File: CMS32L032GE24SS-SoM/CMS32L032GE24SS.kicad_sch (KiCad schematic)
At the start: 9 parts, among them J101 Conn_01x12, J102 Conn_01x12, U101 CMS32L032GE24SS

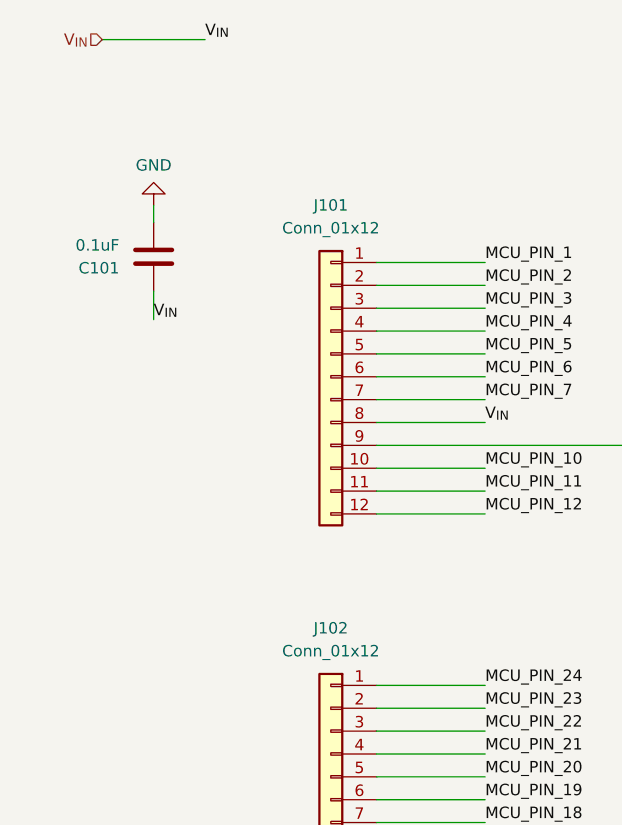
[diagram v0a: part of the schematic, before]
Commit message: basic layout of chips
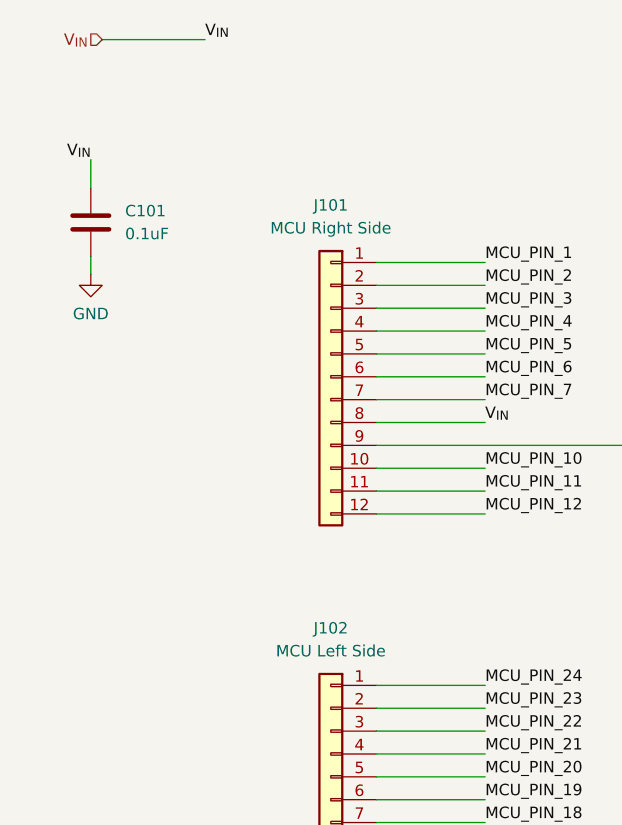
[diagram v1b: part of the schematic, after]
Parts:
- J101: value Conn_01x12 -> MCU Right Side; footprint (none) -> Connector_PinHeader_2.54mm:PinHeader_1x12_P2.54mm_Vertical
- J102: value Conn_01x12 -> MCU Left Side; footprint (none) -> Connector_PinHeader_2.54mm:PinHeader_1x12_P2.54mm_Vertical
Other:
- moved on the sheet: C101
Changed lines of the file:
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@@
     (stroke (width 0) (type default))
   )
-  (wire (pts (xy 34.29 55.88) (xy 34.29 52.705))
+  (wire (pts (xy 27.305 38.1) (xy 27.305 41.275))
     (stroke (width 0) (type default))
   )
@@
     (stroke (width 0) (type default))
   )
-  (wire (pts (xy 34.29 45.085) (xy 34.29 43.18))
+  (wire (pts (xy 27.305 48.895) (xy 27.305 50.8))
     (stroke (width 0) (type default))
   )
@@
     (effects (font (size 1.27 1.27)) (justify left bottom))
   )
-  (label "V_{IN}" (at 34.29 55.88 0) (fields_autoplaced)
-    (effects (font (size 1.27 1.27)) (justify left bottom))
+  (label "V_{IN}" (at 27.305 38.1 180) (fields_autoplaced)
+    (effects (font (size 1.27 1.27)) (justify right bottom))
   )
   (hierarchical_label "V_{IN}" (shape input) (at 28.575 24.765 180) (fields_autoplaced)
@@
     (effects (font (size 1.27 1.27)) (justify left))
   )
-  (symbol (lib_id "Device:C") (at 34.29 48.895 180) (unit 1)
+  (symbol (lib_id "Device:C") (at 27.305 45.085 0) (unit 1)
     (in_bom yes) (on_board yes) (dnp no) (fields_autoplaced)
-    (property "Reference" "C101" (at 30.48 50.165 0)
+    (property "Reference" "C101" (at 31.115 43.815 0)
       (effects (font (size 1.27 1.27)) (justify left))
     )
-    (property "Value" "0.1uF" (at 30.48 47.625 0)
+    (property "Value" "0.1uF" (at 31.115 46.355 0)
       (effects (font (size 1.27 1.27)) (justify left))
     )
-    (property "Footprint" "Capacitor_SMD:C_0805_2012Metric_Pad1.18x1.45mm_HandSolder" (at 33.3248 45.085 0)
-      (effects (font (size 1.27 1.27)) hide)
-    )
-    (property "Datasheet" "~" (at 34.29 48.895 0)
+    (property "Footprint" "Capacitor_SMD:C_0805_2012Metric_Pad1.18x1.45mm_HandSolder" (at 28.2702 48.895 0)
+      (effects (font (size 1.27 1.27)) hide)
+    )
+    (property "Datasheet" "~" (at 27.305 45.085 0)
       (effects (font (size 1.27 1.27)) hide)
     )
@@
     )
   )
-  (symbol (lib_id "power:GND") (at 34.29 43.18 180) (unit 1)
+  (symbol (lib_id "power:GND") (at 27.305 50.8 0) (unit 1)
     (in_bom yes) (on_board yes) (dnp no) (fields_autoplaced)
-    (property "Reference" "#PWR0102" (at 34.29 36.83 0)
-      (effects (font (size 1.27 1.27)) hide)
-    )
-    (property "Value" "GND" (at 34.29 38.735 0)
-      (effects (font (size 1.27 1.27)))
-    )
-    (property "Footprint" "" (at 34.29 43.18 0)
-      (effects (font (size 1.27 1.27)) hide)
-    )
-    (property "Datasheet" "" (at 34.29 43.18 0)
+    (property "Reference" "#PWR0102" (at 27.305 57.15 0)
+      (effects (font (size 1.27 1.27)) hide)
+    )
+    (property "Value" "GND" (at 27.305 55.245 0)
+      (effects (font (size 1.27 1.27)))
+    )
+    (property "Footprint" "" (at 27.305 50.8 0)
+      (effects (font (size 1.27 1.27)) hide)
+    )
+    (property "Datasheet" "" (at 27.305 50.8 0)
       (effects (font (size 1.27 1.27)) hide)
     )
@@
       (effects (font (size 1.27 1.27)))
     )
-    (property "Value" "Conn_01x12" (at 53.975 45.72 0)
-      (effects (font (size 1.27 1.27)))
-    )
-    (property "Footprint" "" (at 53.975 62.23 0)
+    (property "Value" "MCU Right Side" (at 53.975 45.72 0)
+      (effects (font (size 1.27 1.27)))
+    )
+    (property "Footprint" "Connector_PinHeader_2.54mm:PinHeader_1x12_P2.54mm_Vertical" (at 53.975 62.23 0)
       (effects (font (size 1.27 1.27)) hide)
     )
@@
       (effects (font (size 1.27 1.27)))
     )
-    (property "Value" "Conn_01x12" (at 53.975 92.71 0)
-      (effects (font (size 1.27 1.27)))
-    )
-    (property "Footprint" "" (at 53.975 109.22 0)
-      (effects (font (size 1.27 1.27)) hide)
-    )
+    (property "Value" "MCU Left Side" (at 53.975 92.71 0)
+      (effects (font (size 1.27 1.27)))
+    )
+    (property "Footprint" "Connector_PinHeader_2.54mm:PinHeader_1x12_P2.54mm_Vertical" (at 53.975 109.22 0)
+      (effects (font (size 1.27 1.27)) hide)
+    )

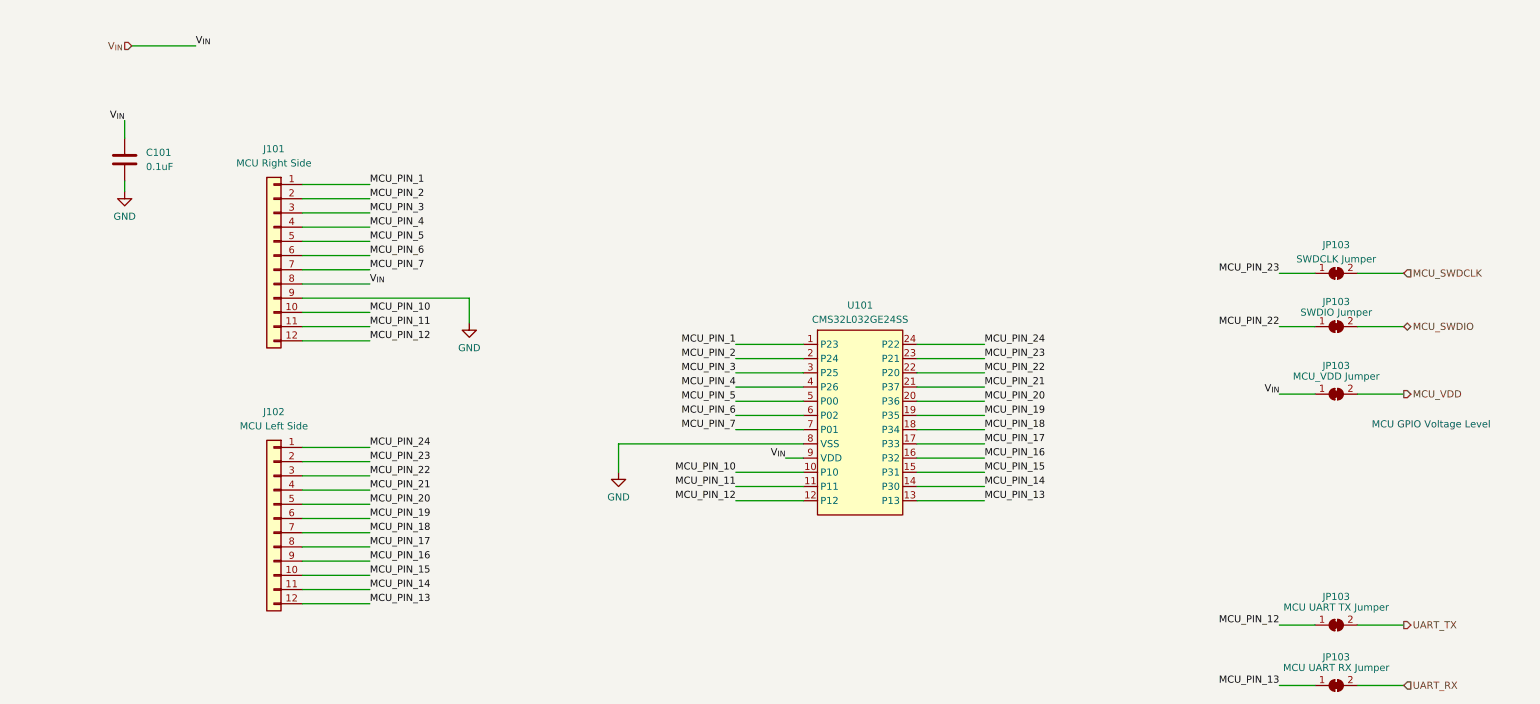
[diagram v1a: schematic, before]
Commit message: locked ArduinoNano board
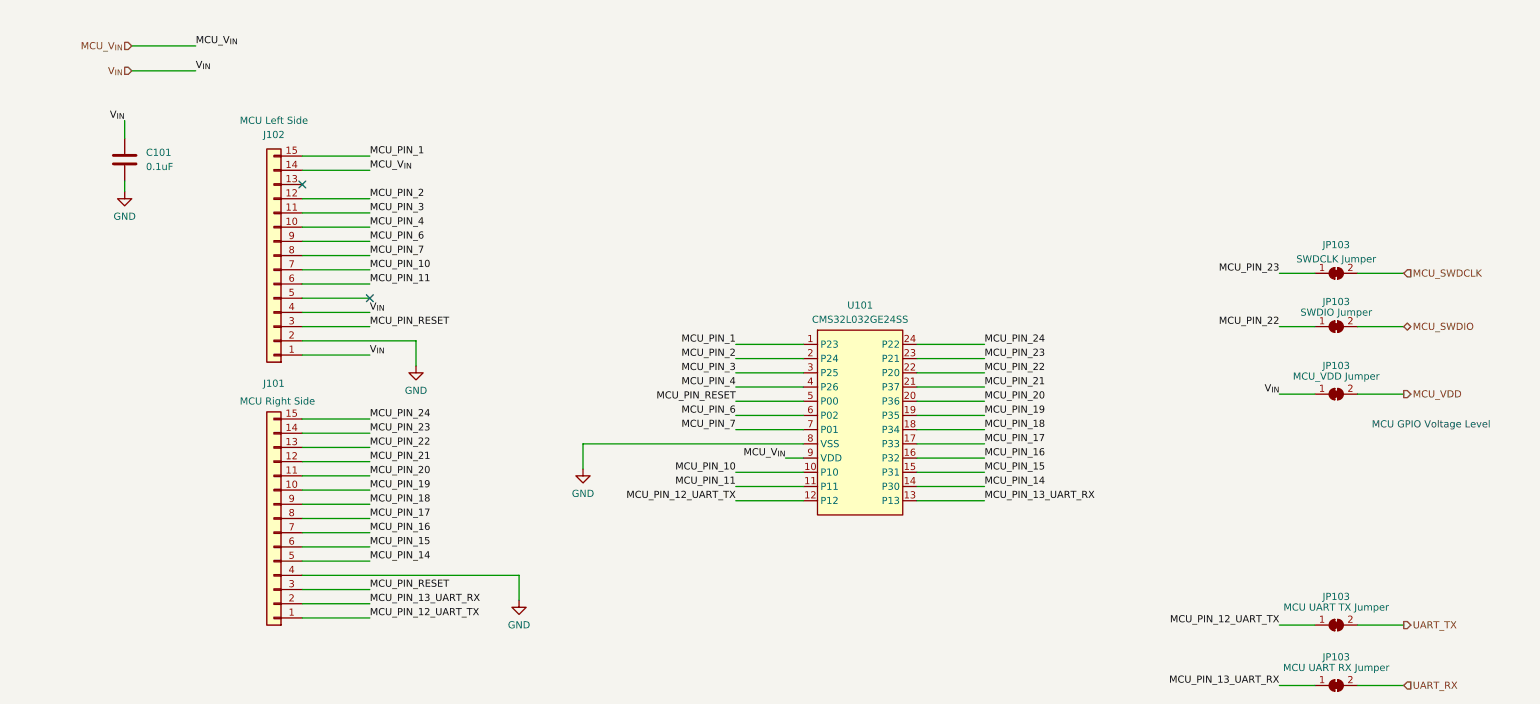
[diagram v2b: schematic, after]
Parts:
- J101, J102: footprint Connector_PinHeader_2.54mm:PinHeader_1x12_P2.54mm_Vertical -> Connector_PinHeader_2.54mm:PinHeader_1x15_P2.54mm_Vertical; symbol Connector_Generic:Conn_01x12 -> Connector_Generic:Conn_01x15
- JP103: footprint Jumper:SolderJumper-2_P1.3mm_Bridged2Bar_RoundedPad1.0x1.5mm -> Jumper:SolderJumper-2_P1.3mm_Bridged_RoundedPad1.0x1.5mm
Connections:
- net GND: now also J101.4 (Pin_4), J102.2 (Pin_2); no longer J101.9 (Pin_9)
- net MCU_PIN_1: now also J102.15 (Pin_15); no longer J101.1 (Pin_1)
- net MCU_PIN_10: now also J102.7 (Pin_7); no longer J101.10 (Pin_10)
- net MCU_PIN_11: now also J102.6 (Pin_6); no longer J101.11 (Pin_11)
- net MCU_PIN_14: now also J101.5 (Pin_5); no longer J102.11 (Pin_11)
- net MCU_PIN_15: now also J101.6 (Pin_6); no longer J102.10 (Pin_10)
- net MCU_PIN_16: now also J101.7 (Pin_7); no longer J102.9 (Pin_9)
- net MCU_PIN_17: now also J101.8 (Pin_8); no longer J102.8 (Pin_8)
- net MCU_PIN_18: now also J101.9 (Pin_9); no longer J102.7 (Pin_7)
- net MCU_PIN_19: now also J101.10 (Pin_10); no longer J102.6 (Pin_6)
- net MCU_PIN_2: now also J102.12 (Pin_12); no longer J101.2 (Pin_2)
- net MCU_PIN_20: now also J101.11 (Pin_11); no longer J102.5 (Pin_5)
- net MCU_PIN_21: now also J101.12 (Pin_12); no longer J102.4 (Pin_4)
- net MCU_PIN_22: now also J101.13 (Pin_13); no longer J102.3 (Pin_3)
- net MCU_PIN_23: now also J101.14 (Pin_14); no longer J102.2 (Pin_2)
- net MCU_PIN_24: now also J101.15 (Pin_15); no longer J102.1 (Pin_1)
- net MCU_PIN_3: now also J102.11 (Pin_11); no longer J101.3 (Pin_3)
- net MCU_PIN_4: now also J102.10 (Pin_10); no longer J101.4 (Pin_4)
- net MCU_PIN_6: now also J102.9 (Pin_9); no longer J101.6 (Pin_6)
- net MCU_PIN_7: now also J102.8 (Pin_8); no longer J101.7 (Pin_7)
- net V_{IN}: now also J102.1 (Pin_1), J102.4 (Pin_4); no longer J101.8 (Pin_8), U101.9 (VDD)
- net MCU_PIN_12 renamed MCU_PIN_12_UART_TX
- net MCU_PIN_12_UART_TX: now also J101.1 (Pin_1); no longer J101.12 (Pin_12)
- net MCU_PIN_13 renamed MCU_PIN_13_UART_RX
- net MCU_PIN_13_UART_RX: now also J101.2 (Pin_2); no longer J102.12 (Pin_12)
- net MCU_PIN_5 renamed MCU_PIN_RESET
- net MCU_PIN_RESET: now also J101.3 (Pin_3), J102.3 (Pin_3); no longer J101.5 (Pin_5)
- new net MCU_V_{IN}: J102.14 (Pin_14), U101.9 (VDD)
- no-connect marks 0 -> 2

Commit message: routing
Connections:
- net MCU_V_{IN}: now also C101.1
- net V_{IN}: no longer C101.1
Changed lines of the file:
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@@
     (effects (font (size 1.27 1.27)) (justify left bottom))
   )
-  (label "V_{IN}" (at 27.305 38.1 180) (fields_autoplaced)
+  (label "MCU_V_{IN}" (at 27.305 38.1 180) (fields_autoplaced)
     (effects (font (size 1.27 1.27)) (justify right bottom))
   )
